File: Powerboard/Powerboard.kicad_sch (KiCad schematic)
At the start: 0 parts

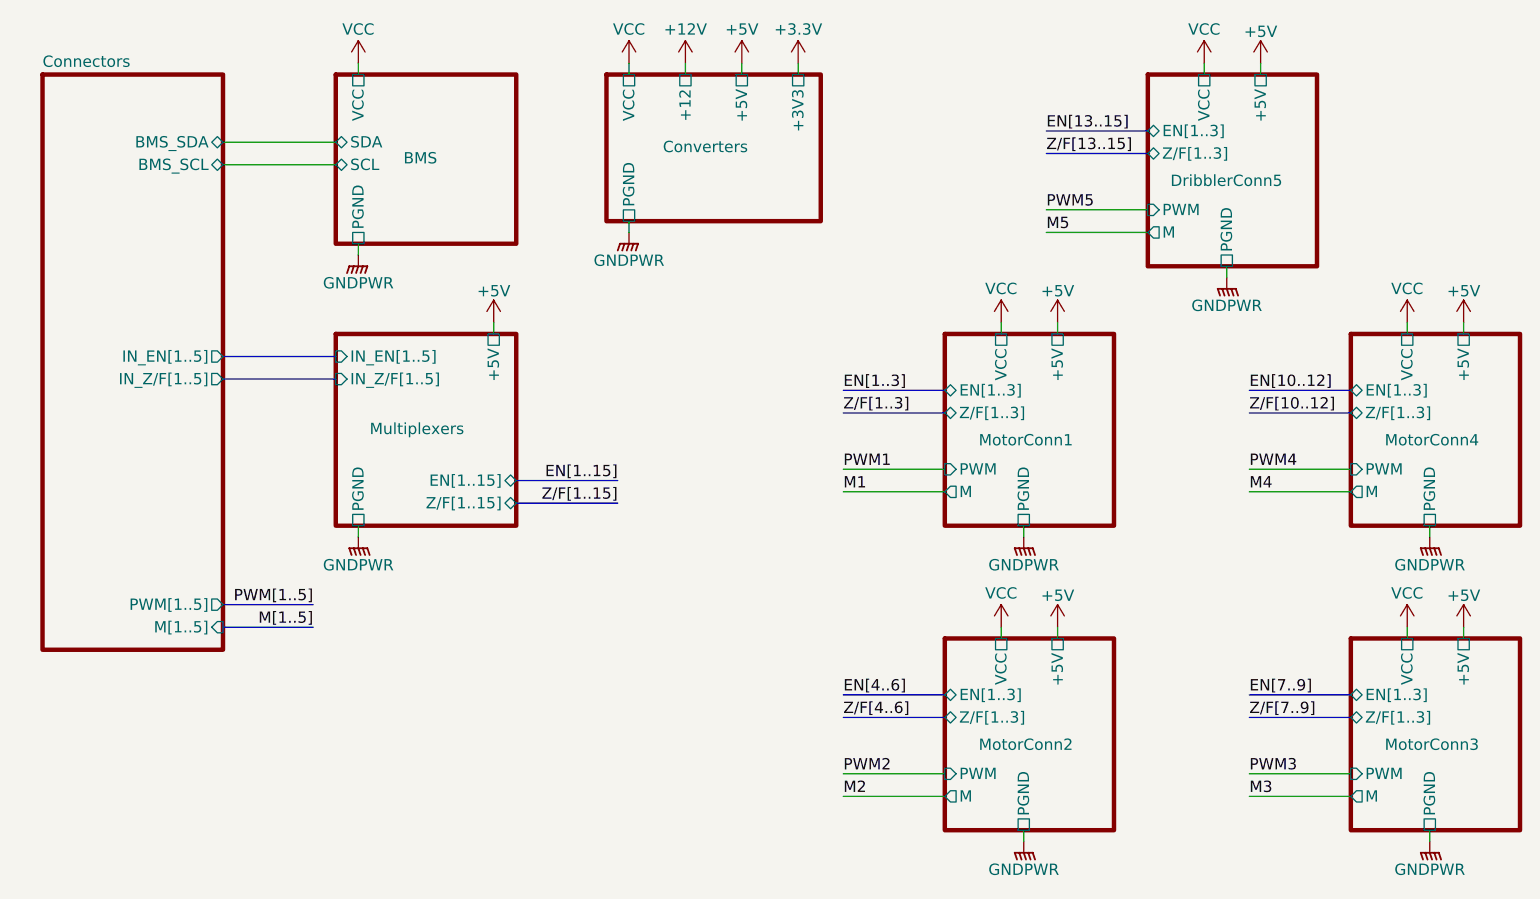
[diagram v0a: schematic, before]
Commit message: DriverboardComp is the complete design, need to be evaluated
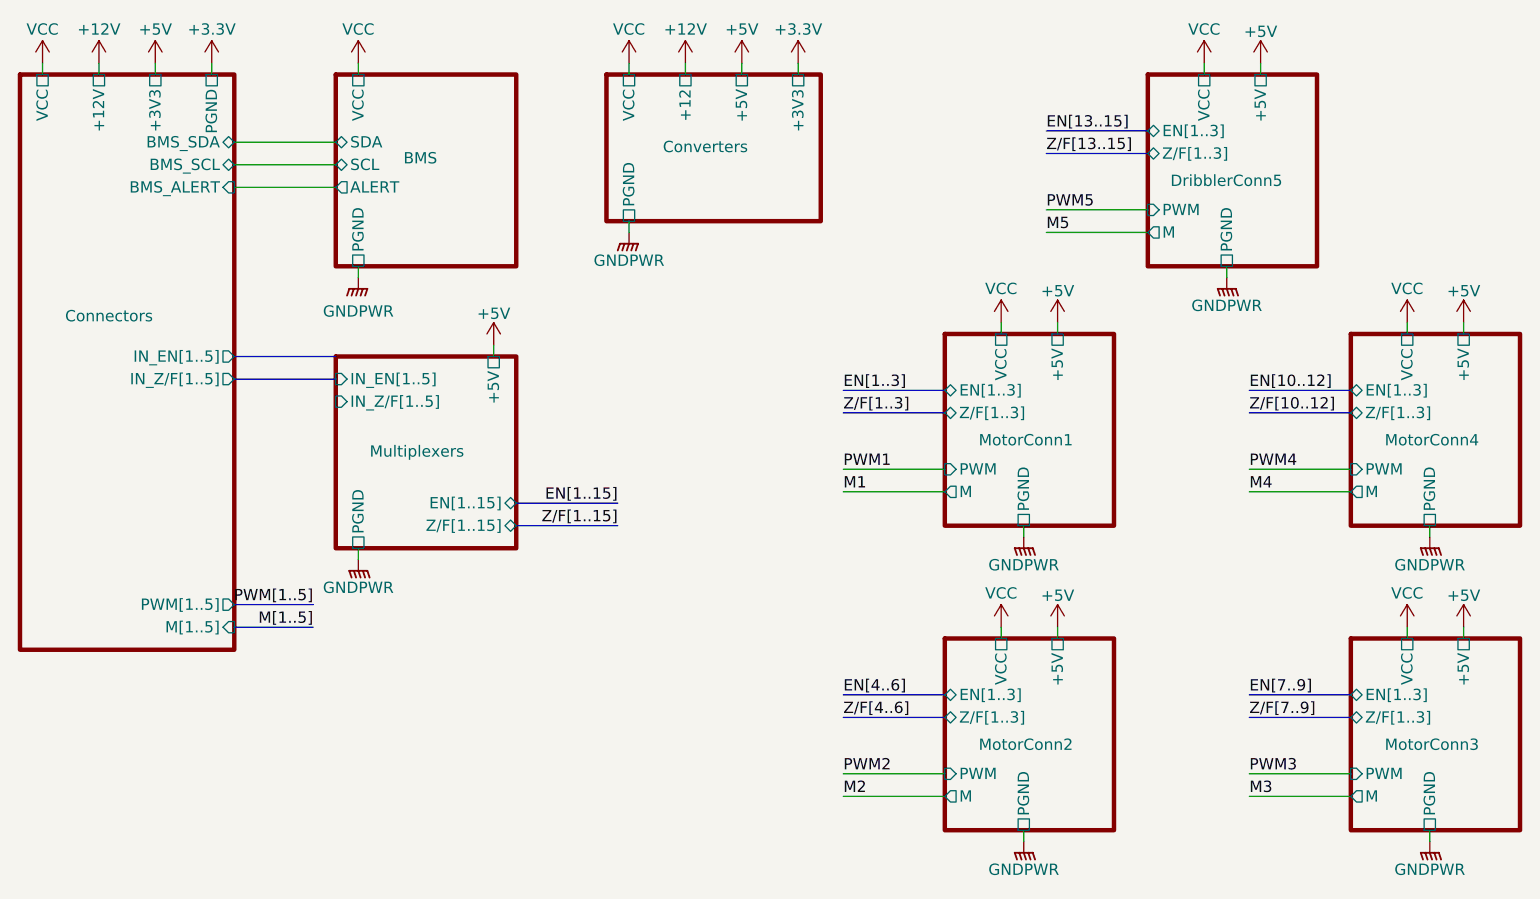
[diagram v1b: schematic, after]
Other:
- sheet BMS ports: added ALERT; removed none
- sheet Connectors ports: added +12V, +3V3, BMS_ALERT, PGND, VCC; removed none
